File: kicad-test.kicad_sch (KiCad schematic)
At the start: 2 parts

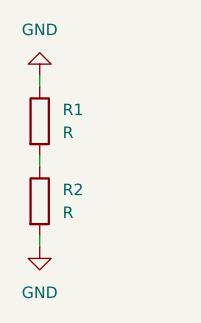
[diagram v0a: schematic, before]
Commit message: added two extra resistors
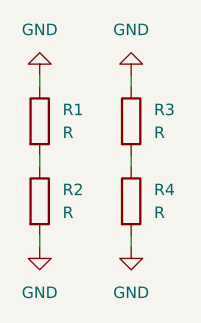
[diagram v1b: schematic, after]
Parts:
- added R3, R4: R, Resistor_SMD:R_1206_3216Metric, symbol Device:R
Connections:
- net GND: now also R3.1, R4.2
- new net: R3.2, R4.1
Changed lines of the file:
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@@
+    (stroke (width 0) (type default))
+  )
+  (wire (pts (xy 80.01 71.12) (xy 80.01 72.39))
+    (stroke (width 0) (type default))
+  )
+  (wire (pts (xy 80.01 53.34) (xy 80.01 54.61))
     (stroke (width 0) (type default))
   )
@@
     (stroke (width 0) (type default))
   )
+  (wire (pts (xy 80.01 62.23) (xy 80.01 63.5))
+    (stroke (width 0) (type default))
+  )
+  (symbol (lib_id "Device:R") (at 80.01 67.31 0) (unit 1)
+    (in_bom yes) (on_board yes) (dnp no) (fields_autoplaced)
+    (property "Reference" "R4" (at 82.55 66.04 0)
+      (effects (font (size 1.27 1.27)) (justify left))
+    )
+    (property "Value" "R" (at 82.55 68.58 0)
+      (effects (font (size 1.27 1.27)) (justify left))
+    )
+    (property "Footprint" "Resistor_SMD:R_1206_3216Metric" (at 78.232 67.31 90)
+      (effects (font (size 1.27 1.27)) hide)
+    )
+    (property "Datasheet" "~" (at 80.01 67.31 0)
+      (effects (font (size 1.27 1.27)) hide)
+    )
+    (pin "1")
+    (pin "2")
+    (instances
+      (project "kicad-test"
+        (path "/2f534111-acb8-4ee5-9e69-1902ade8b997"
+          (reference "R4") (unit 1)
+        )
+      )
+    )
+  )
+  (symbol (lib_id "power:GND") (at 80.01 53.34 180) (unit 1)
+    (in_bom yes) (on_board yes) (dnp no) (fields_autoplaced)
+    (property "Reference" "#PWR03" (at 80.01 46.99 0)
+      (effects (font (size 1.27 1.27)) hide)
+    )
+    (property "Value" "GND" (at 80.01 48.26 0)
+      (effects (font (size 1.27 1.27)))
+    )
+    (property "Footprint" "" (at 80.01 53.34 0)
+      (effects (font (size 1.27 1.27)) hide)
+    )
+    (property "Datasheet" "" (at 80.01 53.34 0)
+      (effects (font (size 1.27 1.27)) hide)
+    )
+    (pin "1")
+    (instances
+      (project "kicad-test"
+        (path "/2f534111-acb8-4ee5-9e69-1902ade8b997"
+          (reference "#PWR03") (unit 1)
+        )
+      )
+    )
+  )
   (symbol (lib_id "Device:R") (at 69.85 58.42 0) (unit 1)
     (in_bom yes) (on_board yes) (dnp no) (fields_autoplaced)
@@
     )
   )
+  (symbol (lib_id "Device:R") (at 80.01 58.42 0) (unit 1)
+    (in_bom yes) (on_board yes) (dnp no) (fields_autoplaced)
+    (property "Reference" "R3" (at 82.55 57.15 0)
+      (effects (font (size 1.27 1.27)) (justify left))
+    )
+    (property "Value" "R" (at 82.55 59.69 0)
+      (effects (font (size 1.27 1.27)) (justify left))
+    )
+    (property "Footprint" "Resistor_SMD:R_1206_3216Metric" (at 78.232 58.42 90)
+      (effects (font (size 1.27 1.27)) hide)
+    )
+    (property "Datasheet" "~" (at 80.01 58.42 0)
+      (effects (font (size 1.27 1.27)) hide)
+    )
+    (pin "2")
+    (pin "1")
+    (instances
+      (project "kicad-test"
+        (path "/2f534111-acb8-4ee5-9e69-1902ade8b997"
+          (reference "R3") (unit 1)
+        )
+      )
+    )
+  )
   (symbol (lib_id "power:GND") (at 69.85 72.39 0) (unit 1)
     (in_bom yes) (on_board yes) (dnp no) (fields_autoplaced)
@@
         )
       )
+    )
+  )
+  (symbol (lib_id "power:GND") (at 80.01 72.39 0) (unit 1)
+    (in_bom yes) (on_board yes) (dnp no) (fields_autoplaced)
+    (property "Reference" "#PWR04" (at 80.01 78.74 0)
+      (effects (font (size 1.27 1.27)) hide)
+    )
+    (property "Value" "GND" (at 80.01 77.47 0)
+      (effects (font (size 1.27 1.27)))
+    )
+    (property "Footprint" "" (at 80.01 72.39 0)
+      (effects (font (size 1.27 1.27)) hide)
+    )
+    (property "Datasheet" "" (at 80.01 72.39 0)
+      (effects (font (size 1.27 1.27)) hide)
+    )
+    (pin "1")
+    (instances
+      (project "kicad-test"
+        (path "/2f534111-acb8-4ee5-9e69-1902ade8b997"
+          (reference "#PWR04") (unit 1)
+        )
+      )

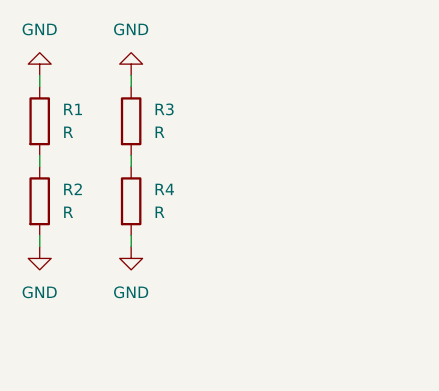
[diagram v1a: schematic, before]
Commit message: added button
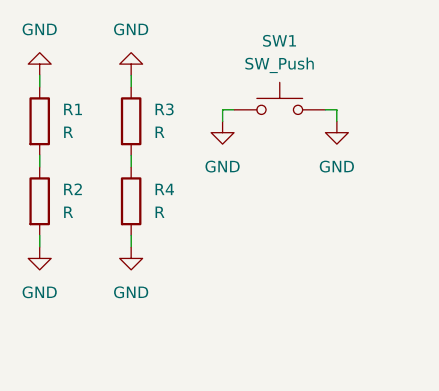
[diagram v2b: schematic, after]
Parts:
- added SW1: SW_Push, Button_Switch_THT:SW_PUSH_6mm_H8mm, symbol Switch:SW_Push
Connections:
- net GND: now also SW1.1, SW1.2
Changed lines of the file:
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@@
+    (stroke (width 0) (type default))
+  )
+  (wire (pts (xy 90.17 57.15) (xy 90.17 58.42))
     (stroke (width 0) (type default))
   )
@@
     (stroke (width 0) (type default))
   )
+  (wire (pts (xy 102.87 58.42) (xy 102.87 57.15))
+    (stroke (width 0) (type default))
+  )
   (wire (pts (xy 80.01 53.34) (xy 80.01 54.61))
     (stroke (width 0) (type default))
@@
     (stroke (width 0) (type default))
   )
+  (wire (pts (xy 102.87 57.15) (xy 101.6 57.15))
+    (stroke (width 0) (type default))
+  )
   (wire (pts (xy 80.01 62.23) (xy 80.01 63.5))
     (stroke (width 0) (type default))
   )
+  (wire (pts (xy 91.44 57.15) (xy 90.17 57.15))
+    (stroke (width 0) (type default))
+  )
+  (symbol (lib_id "Switch:SW_Push") (at 96.52 57.15 0) (unit 1)
+    (in_bom yes) (on_board yes) (dnp no) (fields_autoplaced)
+    (property "Reference" "SW1" (at 96.52 49.53 0)
+      (effects (font (size 1.27 1.27)))
+    )
+    (property "Value" "SW_Push" (at 96.52 52.07 0)
+      (effects (font (size 1.27 1.27)))
+    )
+    (property "Footprint" "Button_Switch_THT:SW_PUSH_6mm_H8mm" (at 96.52 52.07 0)
+      (effects (font (size 1.27 1.27)) hide)
+    )
+    (property "Datasheet" "~" (at 96.52 52.07 0)
+      (effects (font (size 1.27 1.27)) hide)
+    )
+    (pin "2")
+    (pin "1")
+    (instances
+      (project "kicad-test"
+        (path "/2f534111-acb8-4ee5-9e69-1902ade8b997"
+          (reference "SW1") (unit 1)
+        )
+      )
+    )
+  )
+  (symbol (lib_id "power:GND") (at 90.17 58.42 0) (unit 1)
+    (in_bom yes) (on_board yes) (dnp no) (fields_autoplaced)
+    (property "Reference" "#PWR05" (at 90.17 64.77 0)
+      (effects (font (size 1.27 1.27)) hide)
+    )
+    (property "Value" "GND" (at 90.17 63.5 0)
+      (effects (font (size 1.27 1.27)))
+    )
+    (property "Footprint" "" (at 90.17 58.42 0)
+      (effects (font (size 1.27 1.27)) hide)
+    )
+    (property "Datasheet" "" (at 90.17 58.42 0)
+      (effects (font (size 1.27 1.27)) hide)
+    )
+    (pin "1")
+    (instances
+      (project "kicad-test"
+        (path "/2f534111-acb8-4ee5-9e69-1902ade8b997"
+          (reference "#PWR05") (unit 1)
+        )
+      )
+    )
+  )
   (symbol (lib_id "Device:R") (at 80.01 67.31 0) (unit 1)
     (in_bom yes) (on_board yes) (dnp no) (fields_autoplaced)
@@
         )
       )
+    )
+  )
+  (symbol (lib_id "power:GND") (at 102.87 58.42 0) (unit 1)
+    (in_bom yes) (on_board yes) (dnp no) (fields_autoplaced)
+    (property "Reference" "#PWR06" (at 102.87 64.77 0)
+      (effects (font (size 1.27 1.27)) hide)
+    )
+    (property "Value" "GND" (at 102.87 63.5 0)
+      (effects (font (size 1.27 1.27)))
+    )
+    (property "Footprint" "" (at 102.87 58.42 0)
+      (effects (font (size 1.27 1.27)) hide)
+    )
+    (property "Datasheet" "" (at 102.87 58.42 0)
+      (effects (font (size 1.27 1.27)) hide)
+    )
+    (pin "1")
+    (instances
+      (project "kicad-test"
+        (path "/2f534111-acb8-4ee5-9e69-1902ade8b997"
+          (reference "#PWR06") (unit 1)
+        )
+      )

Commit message: added two leds
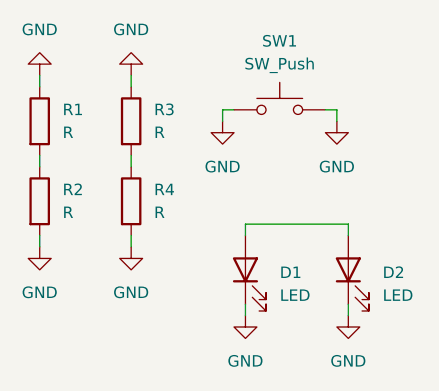
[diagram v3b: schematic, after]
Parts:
- added D1, D2: LED, LED_SMD:LED_1210_3225Metric, symbol Device:LED
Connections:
- net GND: now also D1.1 (K), D2.1 (K)
- new net: D1.2 (A), D2.2 (A)
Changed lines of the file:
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@@
+    (stroke (width 0) (type default))
+  )
+  (wire (pts (xy 104.14 71.12) (xy 104.14 69.85))
     (stroke (width 0) (type default))
   )
@@
     (stroke (width 0) (type default))
   )
+  (wire (pts (xy 104.14 78.74) (xy 104.14 80.01))
+    (stroke (width 0) (type default))
+  )
+  (wire (pts (xy 92.71 69.85) (xy 92.71 71.12))
+    (stroke (width 0) (type default))
+  )
   (wire (pts (xy 102.87 58.42) (xy 102.87 57.15))
     (stroke (width 0) (type default))
@@
     (stroke (width 0) (type default))
   )
+  (wire (pts (xy 104.14 69.85) (xy 92.71 69.85))
+    (stroke (width 0) (type default))
+  )
+  (wire (pts (xy 92.71 78.74) (xy 92.71 80.01))
+    (stroke (width 0) (type default))
+  )
   (wire (pts (xy 91.44 57.15) (xy 90.17 57.15))
     (stroke (width 0) (type default))
@@
     )
   )
+  (symbol (lib_id "power:GND") (at 92.71 80.01 0) (unit 1)
+    (in_bom yes) (on_board yes) (dnp no) (fields_autoplaced)
+    (property "Reference" "#PWR07" (at 92.71 86.36 0)
+      (effects (font (size 1.27 1.27)) hide)
+    )
+    (property "Value" "GND" (at 92.71 85.09 0)
+      (effects (font (size 1.27 1.27)))
+    )
+    (property "Footprint" "" (at 92.71 80.01 0)
+      (effects (font (size 1.27 1.27)) hide)
+    )
+    (property "Datasheet" "" (at 92.71 80.01 0)
+      (effects (font (size 1.27 1.27)) hide)
+    )
+    (pin "1")
+    (instances
+      (project "kicad-test"
+        (path "/2f534111-acb8-4ee5-9e69-1902ade8b997"
+          (reference "#PWR07") (unit 1)
+        )
+      )
+    )
+  )
   (symbol (lib_id "power:GND") (at 80.01 53.34 180) (unit 1)
     (in_bom yes) (on_board yes) (dnp no) (fields_autoplaced)
@@
     )
   )
+  (symbol (lib_id "Device:LED") (at 92.71 74.93 90) (unit 1)
+    (in_bom yes) (on_board yes) (dnp no) (fields_autoplaced)
+    (property "Reference" "D1" (at 96.52 75.2475 90)
+      (effects (font (size 1.27 1.27)) (justify right))
+    )
+    (property "Value" "LED" (at 96.52 77.7875 90)
+      (effects (font (size 1.27 1.27)) (justify right))
+    )
+    (property "Footprint" "LED_SMD:LED_1210_3225Metric" (at 92.71 74.93 0)
+      (effects (font (size 1.27 1.27)) hide)
+    )
+    (property "Datasheet" "~" (at 92.71 74.93 0)
+      (effects (font (size 1.27 1.27)) hide)
+    )
+    (pin "1")
+    (pin "2")
+    (instances
+      (project "kicad-test"
+        (path "/2f534111-acb8-4ee5-9e69-1902ade8b997"
+          (reference "D1") (unit 1)
+        )
+      )
+    )
+  )
   (symbol (lib_id "Device:R") (at 69.85 58.42 0) (unit 1)
     (in_bom yes) (on_board yes) (dnp no) (fields_autoplaced)
@@
     )
   )
+  (symbol (lib_id "power:GND") (at 104.14 80.01 0) (unit 1)
+    (in_bom yes) (on_board yes) (dnp no) (fields_autoplaced)
+    (property "Reference" "#PWR08" (at 104.14 86.36 0)
+      (effects (font (size 1.27 1.27)) hide)
+    )
+    (property "Value" "GND" (at 104.14 85.09 0)
+      (effects (font (size 1.27 1.27)))
+    )
+    (property "Footprint" "" (at 104.14 80.01 0)
+      (effects (font (size 1.27 1.27)) hide)
+    )
+    (property "Datasheet" "" (at 104.14 80.01 0)
+      (effects (font (size 1.27 1.27)) hide)
+    )
+    (pin "1")
+    (instances
+      (project "kicad-test"
+        (path "/2f534111-acb8-4ee5-9e69-1902ade8b997"
+          (reference "#PWR08") (unit 1)
+        )
+      )
+    )
+  )
   (symbol (lib_id "power:GND") (at 69.85 53.34 180) (unit 1)
     (in_bom yes) (on_board yes) (dnp no) (fields_autoplaced)
@@
         )
       )
+    )
+  )
+  (symbol (lib_id "Device:LED") (at 104.14 74.93 90) (unit 1)
+    (in_bom yes) (on_board yes) (dnp no) (fields_autoplaced)
+    (property "Reference" "D2" (at 107.95 75.2475 90)
+      (effects (font (size 1.27 1.27)) (justify right))
+    )
+    (property "Value" "LED" (at 107.95 77.7875 90)
+      (effects (font (size 1.27 1.27)) (justify right))
+    )
+    (property "Footprint" "LED_SMD:LED_1210_3225Metric" (at 104.14 74.93 0)
+      (effects (font (size 1.27 1.27)) hide)
+    )
+    (property "Datasheet" "~" (at 104.14 74.93 0)
+      (effects (font (size 1.27 1.27)) hide)
+    )
+    (pin "1")
+    (pin "2")
+    (instances
+      (project "kicad-test"
+        (path "/2f534111-acb8-4ee5-9e69-1902ade8b997"
+          (reference "D2") (unit 1)
+        )
+      )
